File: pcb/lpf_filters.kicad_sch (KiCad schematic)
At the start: 73 parts

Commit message: Rev C layout: board grown to 130x110 mm, headers J4/J5/J8/J10/J14 removed, power rework layout
- Outline grown 10 mm on top and left edges (130x110 mm); locked edge parts moved with outline
- Removed J4, J5, J8, J10, J14 and support parts (D13-D15, D17, D19, D20, R64-R67, R69-R71, R75-R79); UPDI J13 kept
- Power rework placed and routed (TPS61085 boost, INA193 U14, Q10 soft-start)
- Y1 placed at U9, stray passives moved, silkscreen labels cleaned up
- Routed: DRC 0 errors / 0 unconnected, schematic parity 0, ERC 0; layout gate 11/11
- DRU: ESC_* fine-pitch escape 0.20 mm rule areas, U1 pad-to-pad 0.14 mm
- In2 keep-away waivers (GND-plane shielded): Q2 drain, MCU_TX, MCU_RX near R6, 22.6 mm MCU_RX run near U9
- Libs: 6x6 H13 switch, OLED pin-header module footprint, updated symbols
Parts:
- C202: LCSC C28262 -> C527065; MPN CL10C680JB8NNNC -> CC0603JRNPO0BN680; Manufacturer Samsung Electro-Mechanics -> YAGEO
- C204, C215, C217, C218: LCSC C14858 -> C107033; MPN CL10C101JB8NNNC -> CC0603JRNPO0BN101; Manufacturer Samsung Electro-Mechanics -> YAGEO
- C216: LCSC C1664 -> C327088; MPN CL10C331JB8NNNC -> CC0603JRNPO0BN331; Manufacturer Samsung Electro-Mechanics -> YAGEO

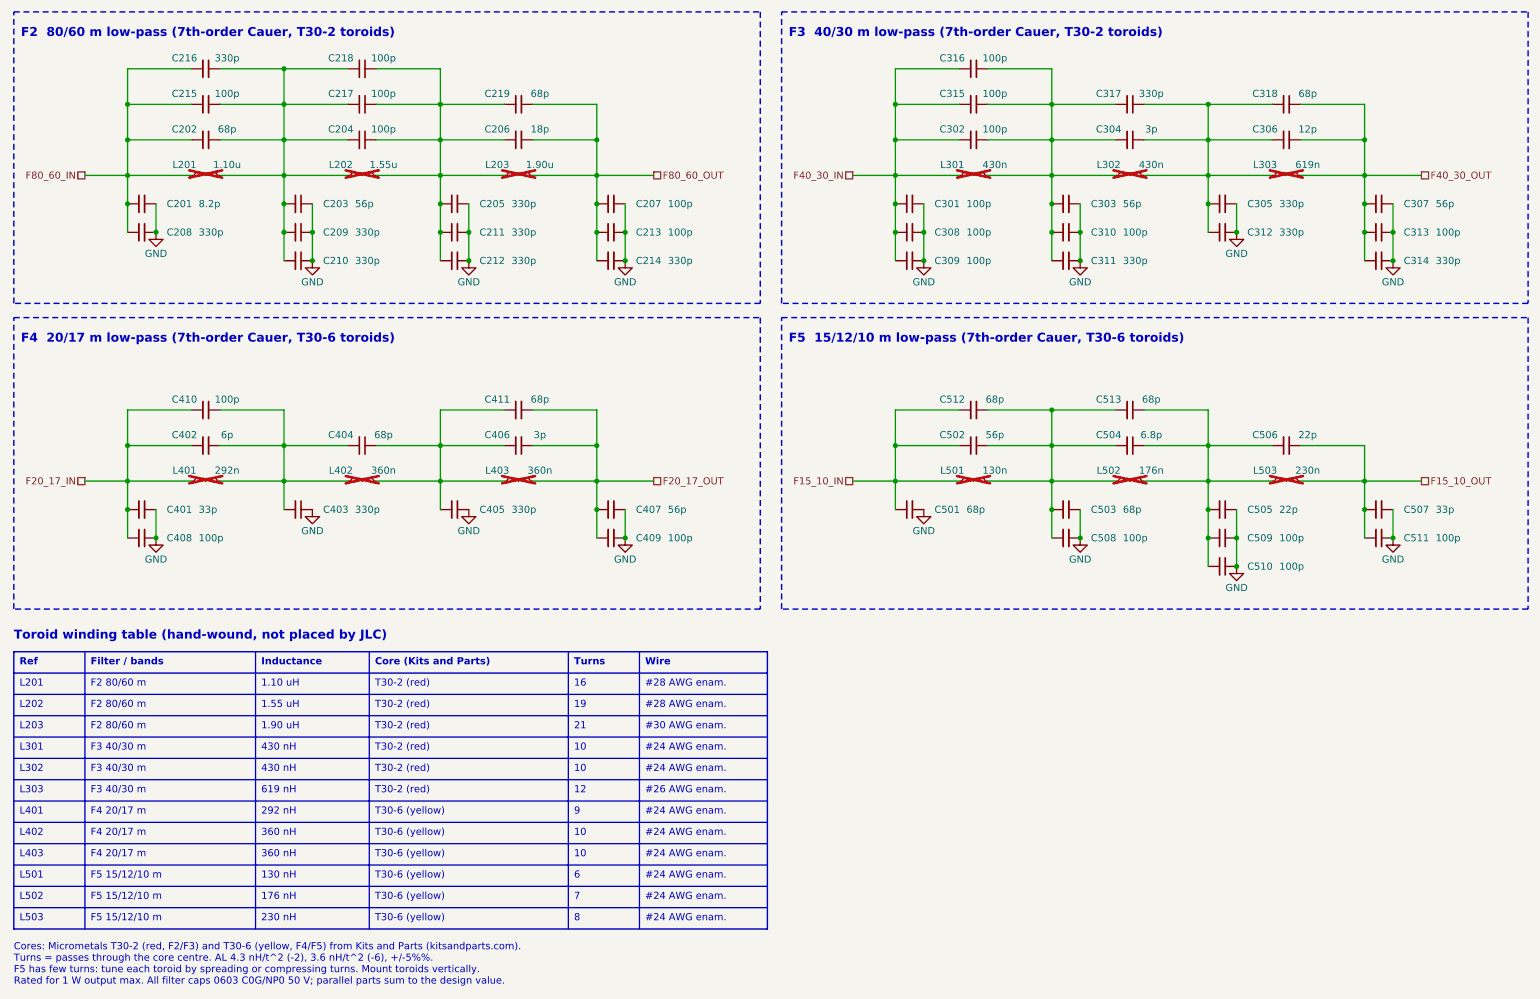
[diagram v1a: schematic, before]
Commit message: Renumber all references monotonically 1..N per prefix; sync PCB silk labels and auto-named nets; ERC 0, DRC 0/0
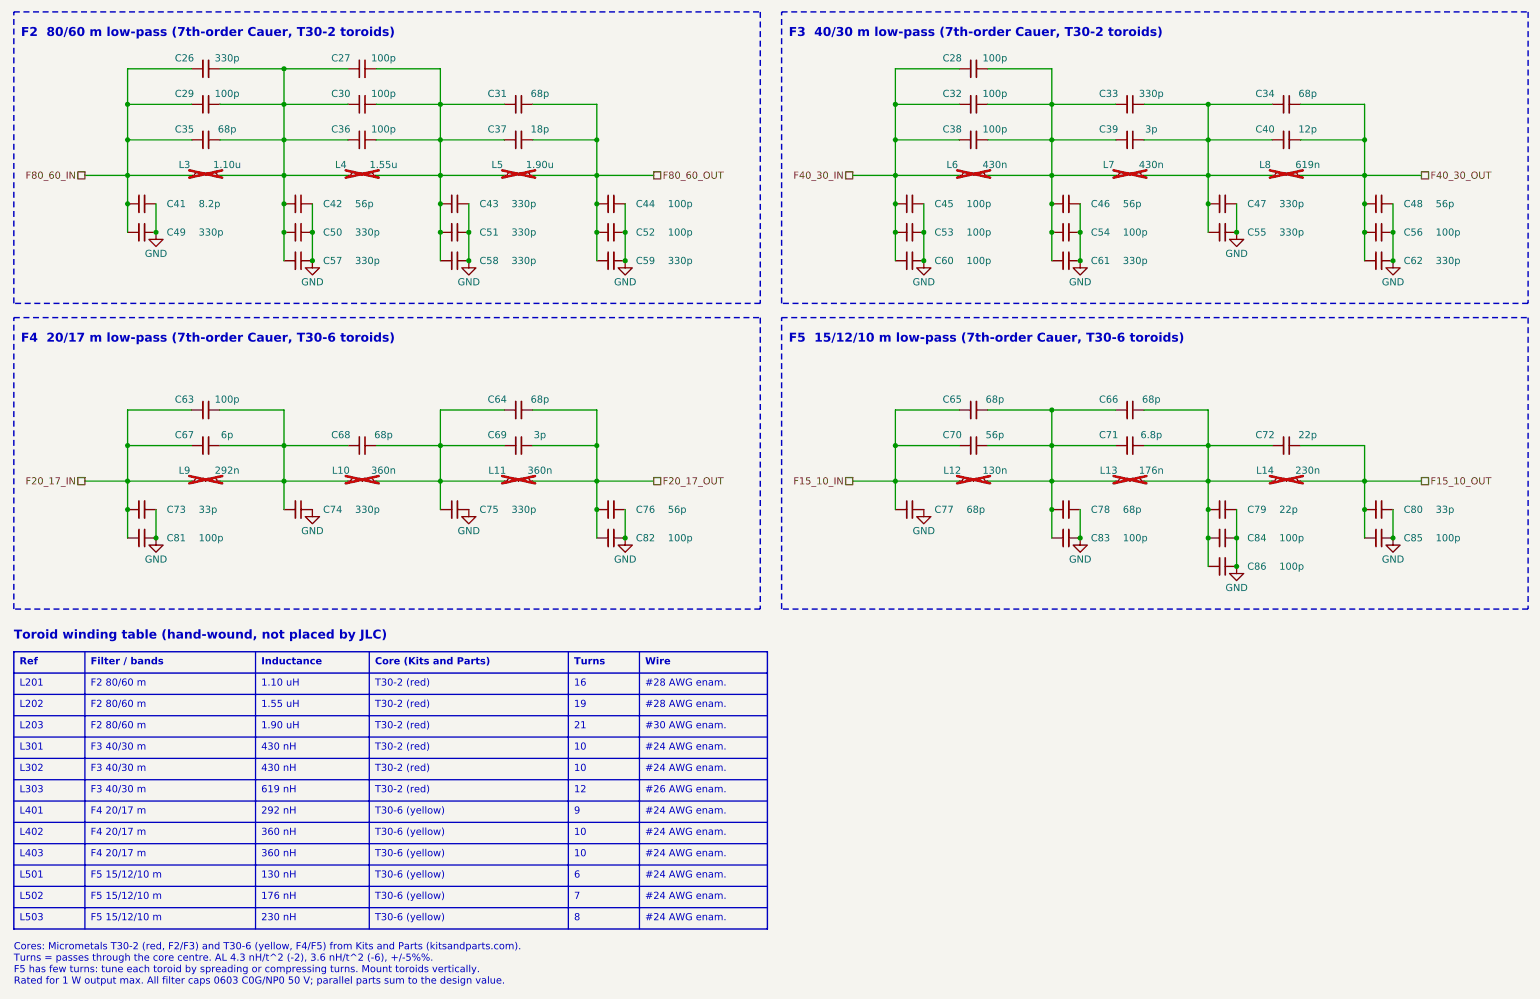
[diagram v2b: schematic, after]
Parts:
- renumbered C216 to C26, C218 to C27, C316 to C28, C215 to C29, C217 to C30, C219 to C31, C315 to C32, C317 to C33, C318 to C34, C202 to C35, C204 to C36, C206 to C37, C302 to C38, C304 to C39, C306 to C40, C201 to C41, C203 to C42, C205 to C43, C207 to C44, C301 to C45, C303 to C46, C305 to C47, C307 to C48, C208 to C49, C209 to C50, C211 to C51, C213 to C52, C308 to C53, C310 to C54, C312 to C55, C313 to C56, C210 to C57, C212 to C58, C214 to C59, C309 to C60, C311 to C61, C314 to C62, C410 to C63, C411 to C64, C512 to C65, C513 to C66, C402 to C67, C404 to C68, C406 to C69, C502 to C70, C504 to C71, C506 to C72, C401 to C73, C403 to C74, C405 to C75, C407 to C76, C501 to C77, C503 to C78, C505 to C79, C507 to C80, C408 to C81, C409 to C82, C508 to C83, C509 to C84, C511 to C85, C510 to C86, L402 to L10, L403 to L11, L501 to L12, L502 to L13, L503 to L14, L201 to L3, L202 to L4, L203 to L5, L301 to L6, L302 to L7, L303 to L8, L401 to L9
